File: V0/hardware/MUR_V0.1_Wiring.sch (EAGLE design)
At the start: 19 parts, among them M1 IN_VALVE, M2 OUT_VALVE, M3 OVERPRESSURE_VALVE, T1 2N3904, X1 MKDSN1,5/2-5,08

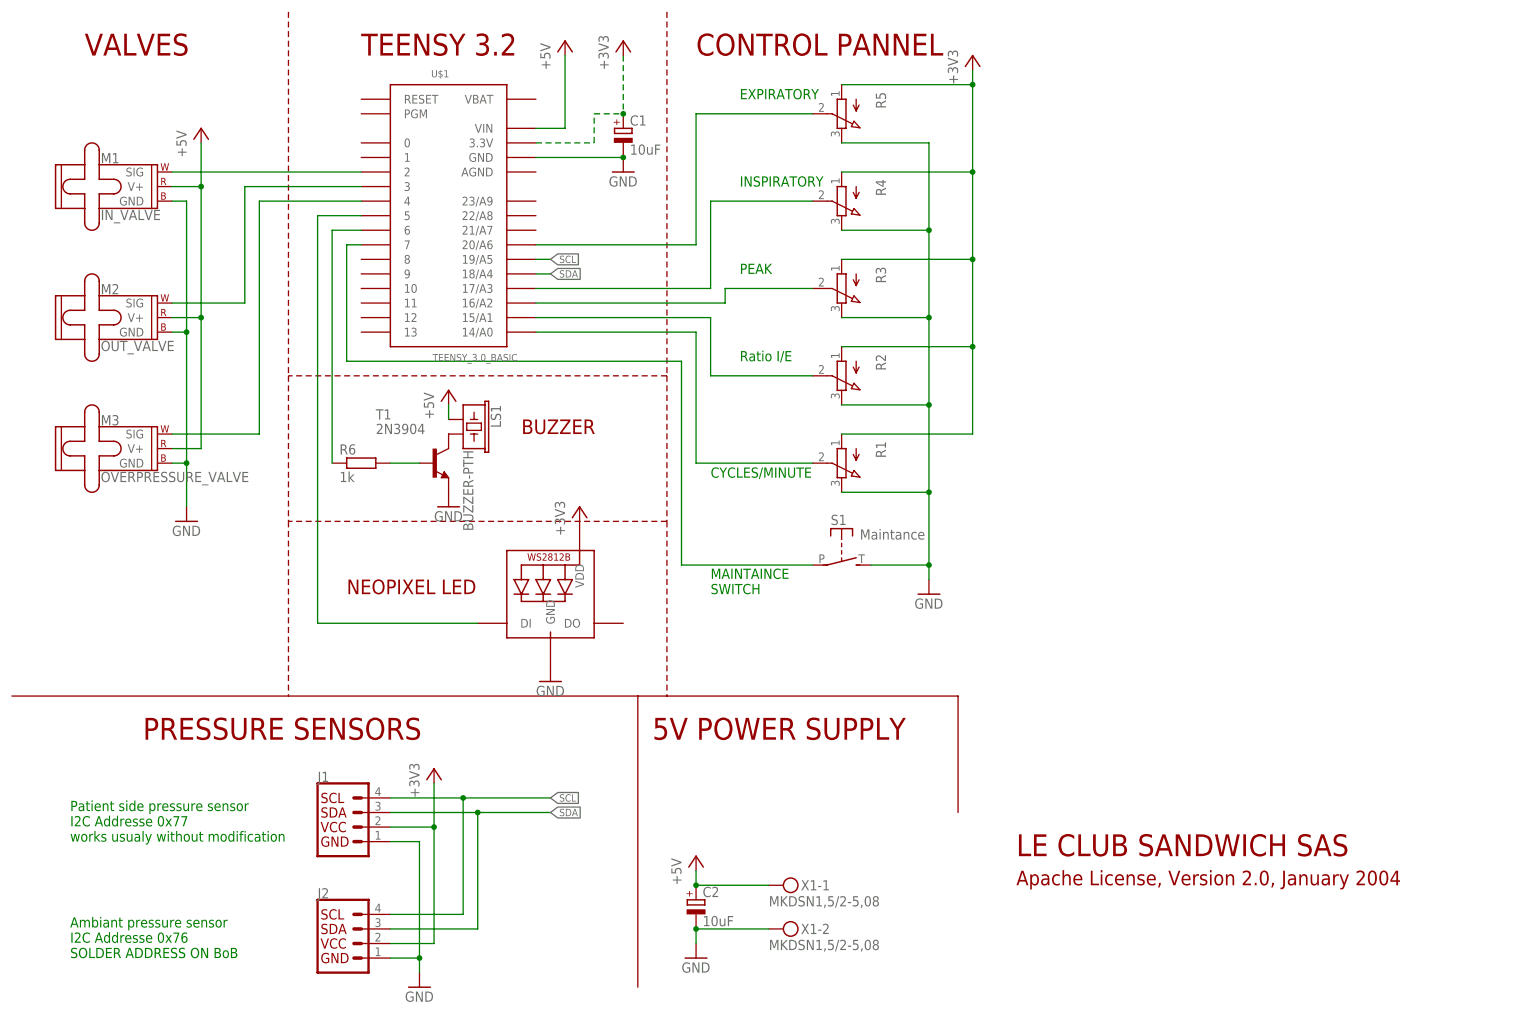
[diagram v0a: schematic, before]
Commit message: better calibration procedure and other improvements
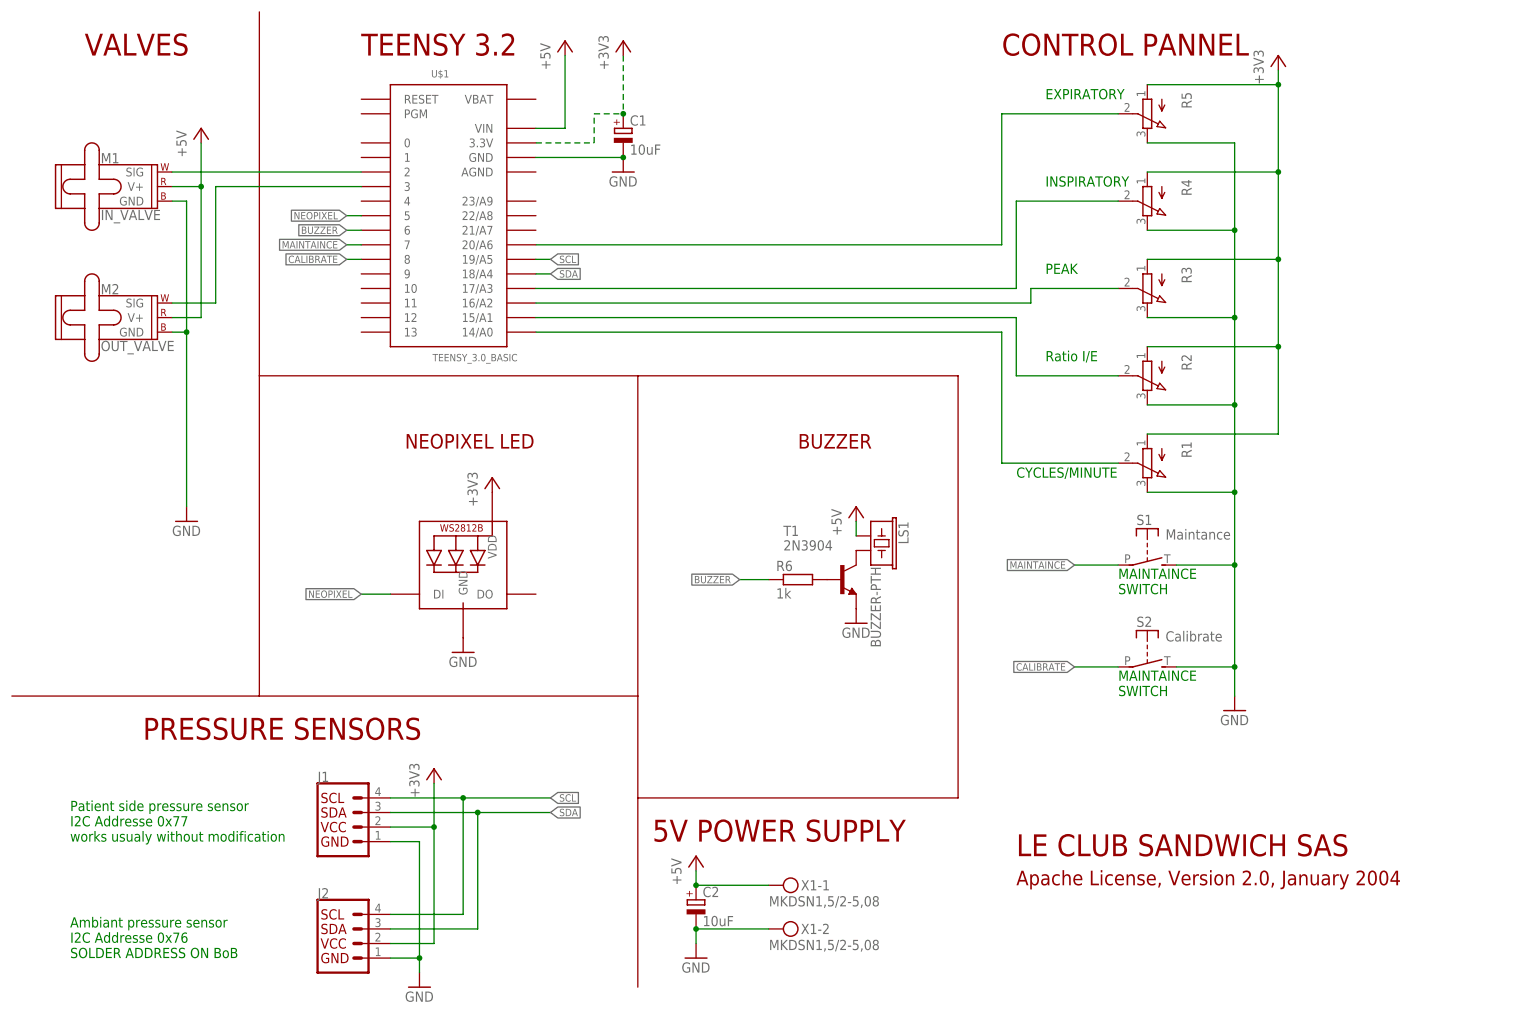
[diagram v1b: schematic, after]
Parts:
- removed M3: OVERPRESSURE_VALVE, SparkFun-Electromechanical:SERVO
- added S2: Calibrate, adafruit:SPST
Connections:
- net N$12 renamed BUZZER
- net N$13 renamed NEOPIXEL
- net N$5 renamed MAINTAINCE
- removed net N$3: M3.SIG, U$1.4
- new net CALIBRATE: S2.P, U$1.8
- net +5V: no longer M3.V+
- net GND: now also S2.S; no longer M3.GND
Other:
- moved on the sheet: LS1, R1, R2, R3, R4, R5, R6, S1, T1
